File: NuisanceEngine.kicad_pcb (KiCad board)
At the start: 2 copper layers, 60 x 53 mm, 58 parts, among them J1 CV, J2 Headphones, J3 Power, Q1 2N3904, Q2 2N3904, Q3 TIP31A, Q4 TIP32A, SW1 SW_SPDT, SW2 SW_SPDT, U1 LM324

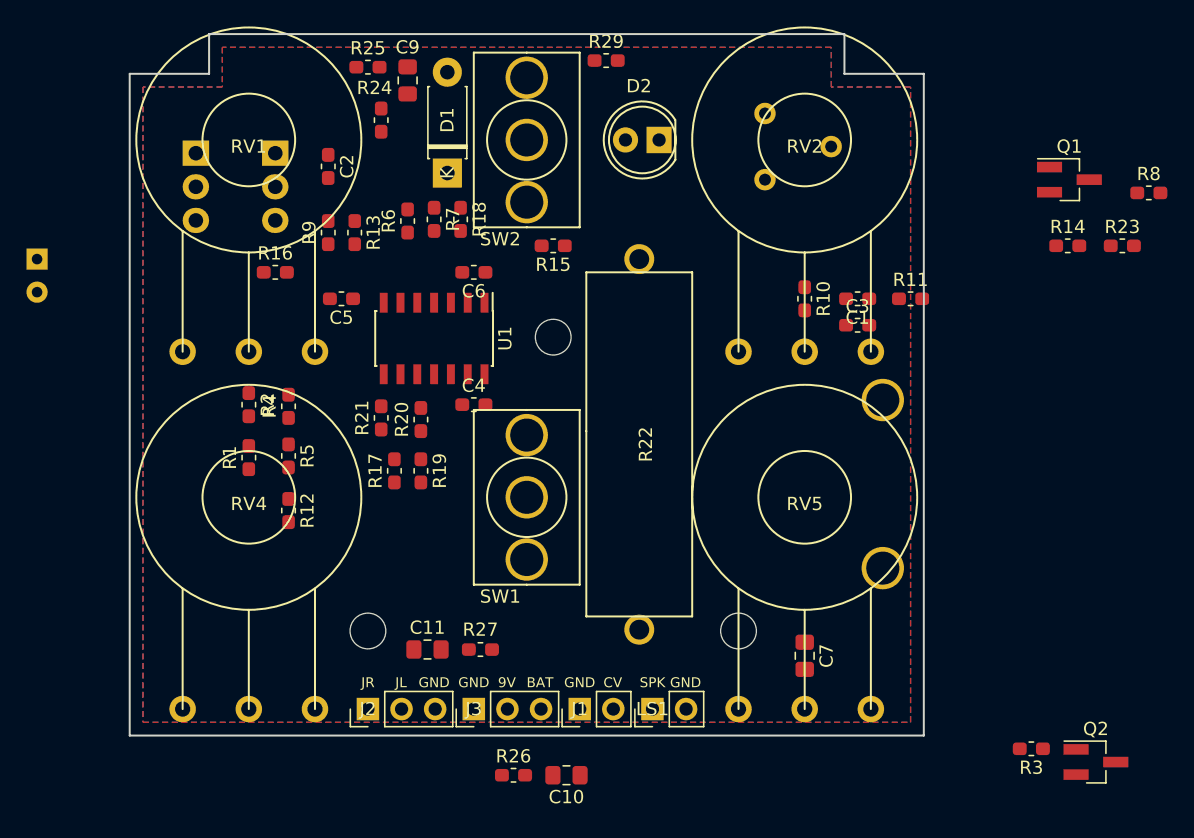
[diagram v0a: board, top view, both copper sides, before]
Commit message: Laid out SMT components, ready for traces
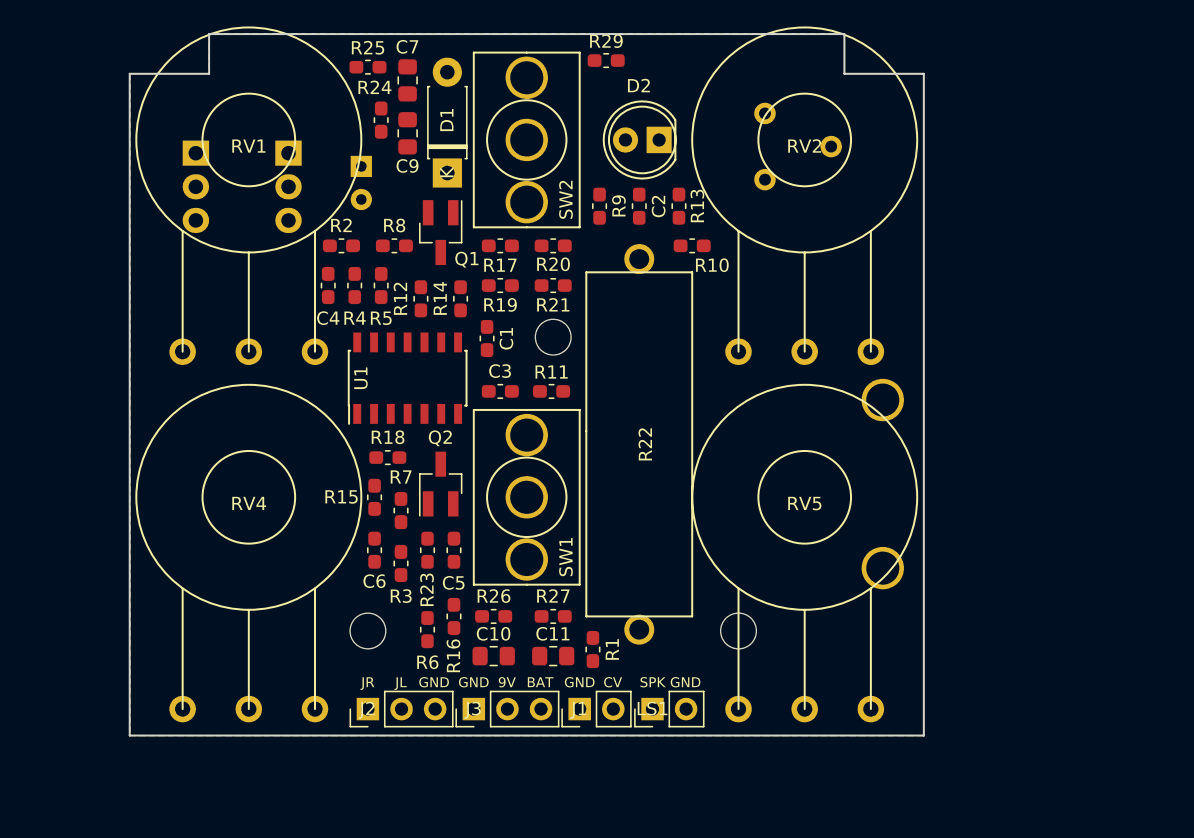
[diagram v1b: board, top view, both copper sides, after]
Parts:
- moved R23 57.3 mm to (72.5, 86.0), turned to 90 degrees
- moved R8 57.1 mm to (70.0, 63.0), turned to 180 degrees
- moved Q2 53.8 mm to (73.5, 81.0), turned to 90 degrees
- moved C7 52.8 mm to (71.0, 50.5), turned to 90 degrees
- moved R3 49.6 mm to (70.5, 87.0), turned to 270 degrees
- moved Q1 47.7 mm to (73.5, 62.0), turned to 270 degrees
- moved R14 46.0 mm to (75.0, 67.0), turned to 270 degrees
- moved R6 30.9 mm to (72.5, 92.0), turned to 270 degrees
- moved R1 29.8 mm to (85.0, 93.5)
- moved R16 29.3 mm to (74.5, 91.0), turned to 270 degrees
- moved C1 28.2 mm to (77.0, 70.0), turned to 90 degrees
- moved R11 28.0 mm to (81.9, 74.0)
- moved C3 27.5 mm to (78.0, 74.0)
- moved C8 25.5 mm to (67.5, 57.0)
- moved R13 24.6 mm to (91.5, 60.0)
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
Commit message: Dunzo
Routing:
- net Net-(C6-Pad1): track 0.00 -> 177.4 mm
- net Net-(C7-Pad2): track 0.00 -> 86.0 mm
- net Net-(C3-Pad1): track 0.00 -> 69.6 mm
- net VDD: track 0.00 -> 67.5 mm
- net Net-(C6-Pad2): track 0.00 -> 45.9 mm, vias 0 -> 2
- net Net-(J3-Pad2): track 0.00 -> 43.5 mm
- net Net-(R1-Pad2): track 0.00 -> 43.0 mm, vias 0 -> 2
- net Net-(BT1-Pad1): track 0.00 -> 36.2 mm
- net Net-(R22-Pad1): track 0.00 -> 35.6 mm
- net Net-(C4-Pad1): track 0.00 -> 35.6 mm
- net Net-(C1-Pad2): track 0.00 -> 32.4 mm
- net Net-(R14-Pad2): track 0.00 -> 31.9 mm, vias 0 -> 2
- net Net-(C8-Pad2): track 0.00 -> 27.7 mm
- net Net-(C7-Pad1): track 0.00 -> 22.6 mm
- net Net-(R3-Pad2): track 0.00 -> 20.3 mm
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
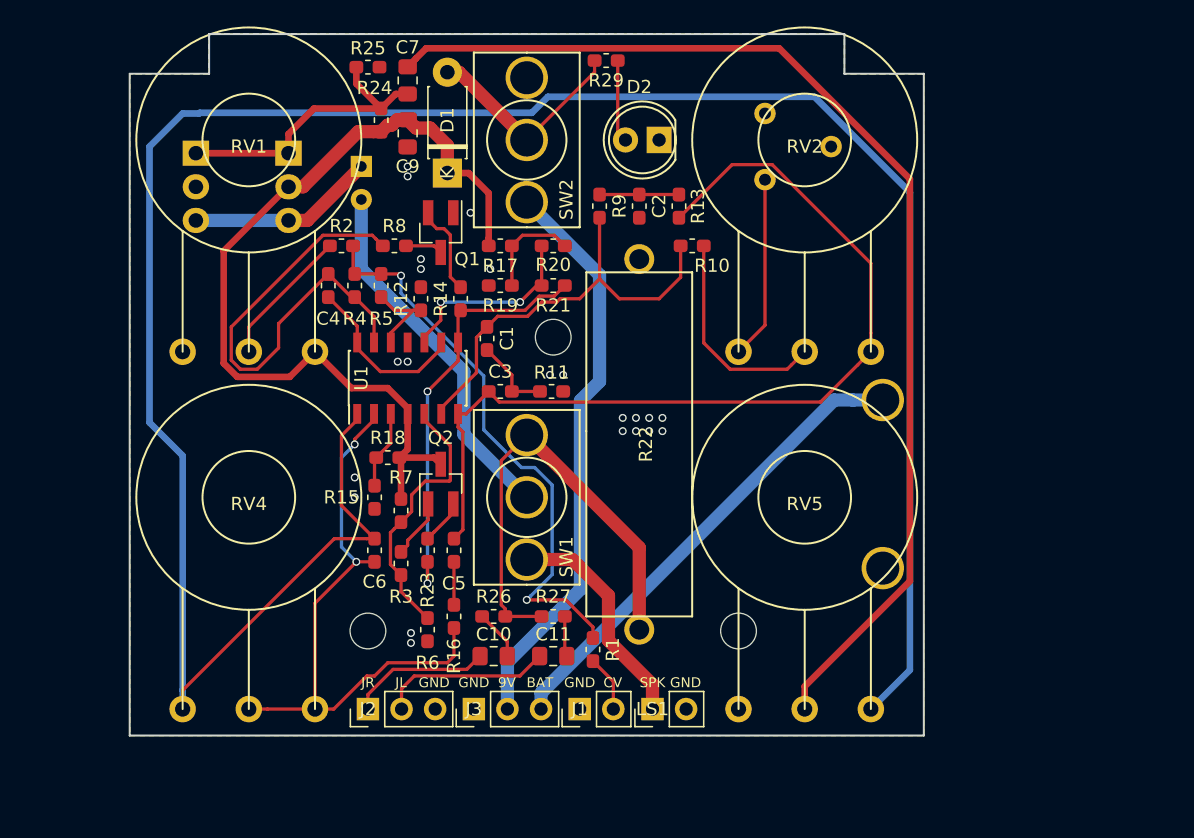
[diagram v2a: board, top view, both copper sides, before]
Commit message: Commit before changing pot footprint
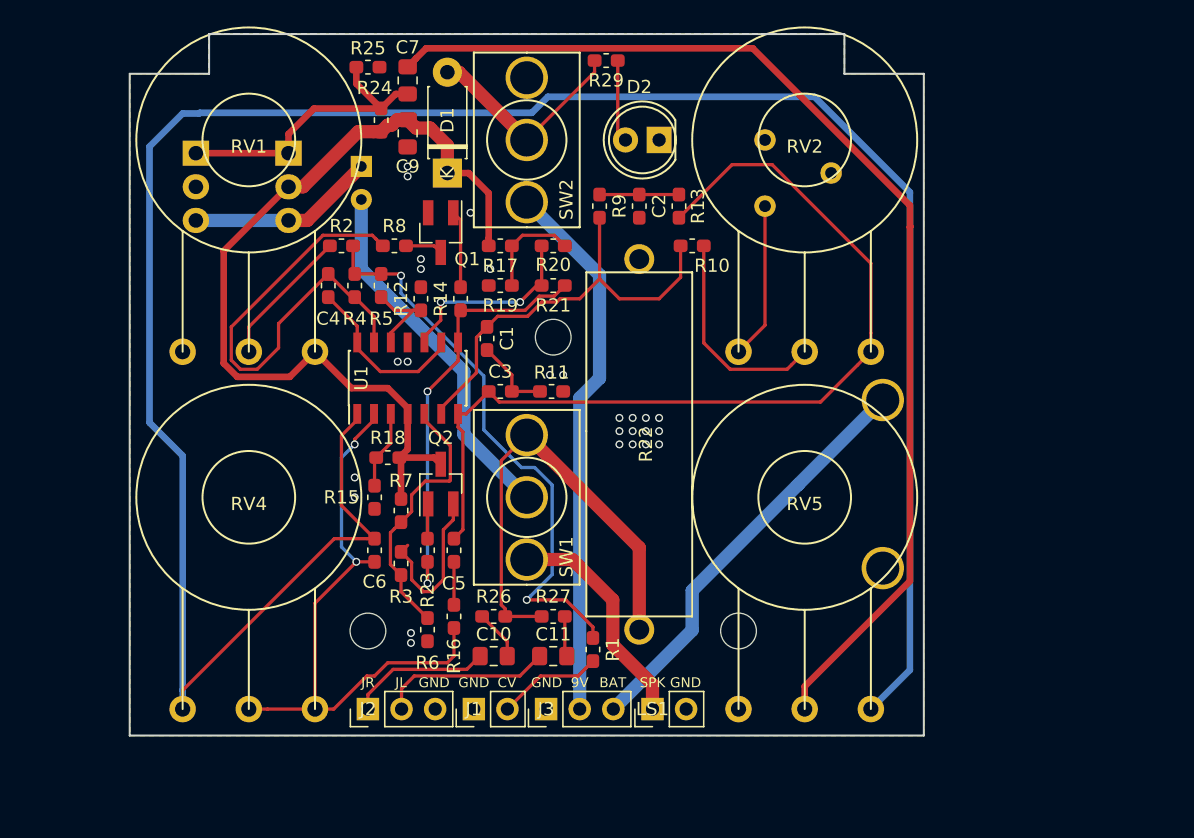
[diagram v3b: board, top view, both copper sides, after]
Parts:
- added LOGO: , HammerheadAudio:HHLOGO, B.Cu at (64.5, 47.5)
- C4: value .047uf -> 0.047uf
- moved J1 8.00 mm to (76.0, 98.0)
- moved J3 5.46 mm to (81.5, 98.0)
- moved RV3 2.00 mm to (98.0, 55.0)
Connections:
- Q1 pad 1: GND -> Net-(Q1-Pad1)
- Q1 pad 2: Net-(Q1-Pad2) -> GND
- R14 pad 1: Net-(Q1-Pad2) -> Net-(Q1-Pad1)
- R23 pad 2: Net-(Q2-Pad2) -> Net-(Q2-Pad1)
- R3 pad 1: Net-(Q2-Pad1) -> Net-(Q2-Pad2)
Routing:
- net Net-(Q2-Pad2): track 3.43 -> 13.0 mm
- net Net-(Q1-Pad2): track 6.96 -> 0.00 mm
- net Net-(Q1-Pad1): track 0.00 -> 5.85 mm
- net Net-(BT1-Pad1): track 36.2 -> 31.8 mm
- net Net-(J1-Pad2): track 4.26 -> 7.96 mm
- net Net-(J3-Pad2): track 43.5 -> 41.2 mm
- net Net-(RV2-Pad1): track 13.8 -> 11.8 mm
- net Net-(Q2-Pad1): track 4.47 -> 2.65 mm
- net Net-(C7-Pad2): track 86.0 -> 84.9 mm
- net GND: track 0.45 -> 1.00 mm, vias 22 -> 26
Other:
- board text added: "Adjust Min Resonance"
- board text added: "Nuisance Engine V1.0 Emmett Palaima Hammerhead Audio 2019"

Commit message: new pot footprint
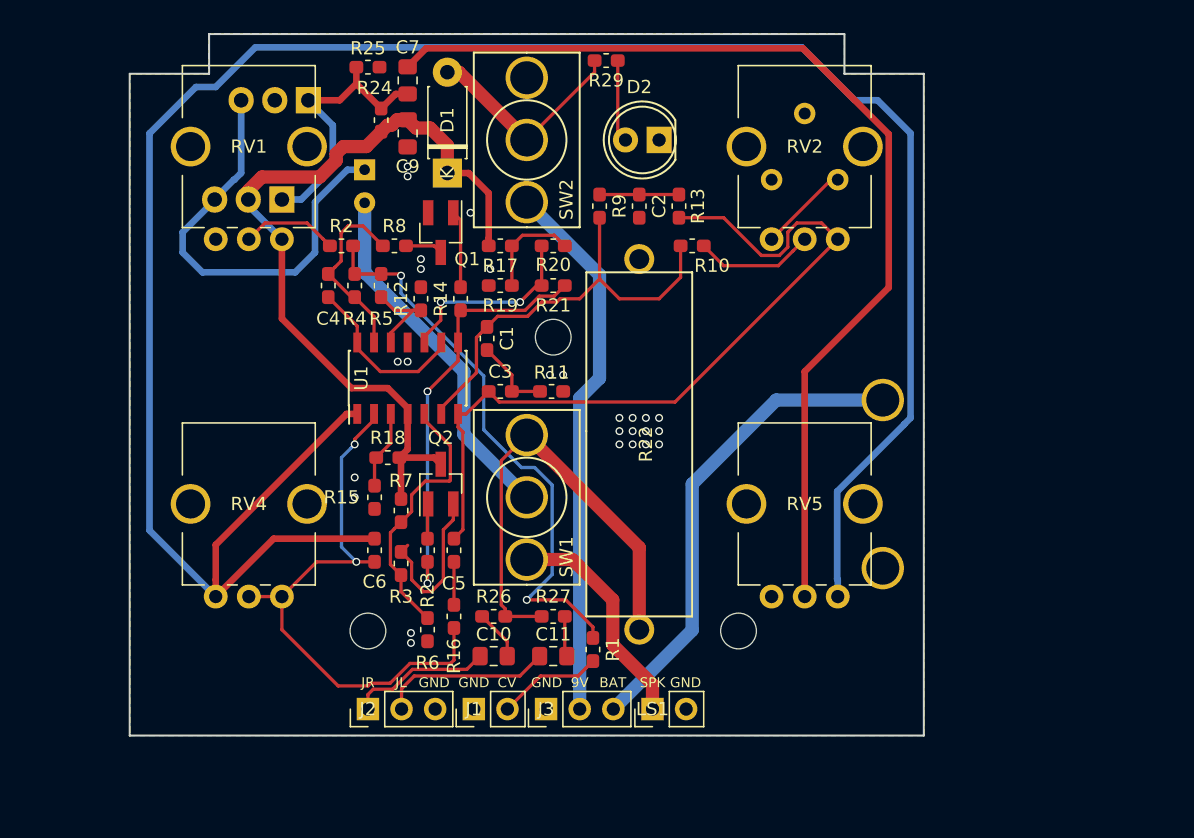
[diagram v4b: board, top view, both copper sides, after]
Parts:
- RV1, RV2, RV4, RV5: footprint HammerheadAudio:Alpha_Pot_16MM -> HammerheadAudio:PTV09
- moved Q4 9.39 mm to (63.5, 52.0), turned to 180 degrees
- moved Q3 3.54 mm to (61.5, 59.5), turned to 180 degrees
- moved RV3 3.04 mm to (98.5, 58.0), turned to 90 degrees
- moved C8 0.35 mm to (67.8, 57.2)
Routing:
- net Net-(C4-Pad1): track 35.6 -> 14.2 mm
- net Net-(C8-Pad1): track 14.2 -> 33.2 mm
- net Net-(C3-Pad1): track 69.6 -> 60.0 mm
- net Net-(C7-Pad2): track 84.9 -> 77.2 mm
- net Net-(C6-Pad1): track 177.4 -> 169.8 mm
- net Net-(R10-Pad2): track 16.3 -> 9.07 mm
- net VDD: track 67.5 -> 61.7 mm
- net Net-(RV2-Pad1): track 11.8 -> 6.86 mm
- net Net-(BT1-Pad1): track 31.8 -> 36.5 mm
- net Net-(R2-Pad1): track 10.5 -> 7.35 mm
- net Net-(C6-Pad2): track 45.9 -> 43.9 mm
- net Net-(C7-Pad1): track 22.6 -> 21.2 mm
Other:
- board text added: "Nuisance Engine V1.1 Emmett Palaima Hammerhead Audio 2019"
- board text removed: "Nuisance Engine V1.0 Emmett Palaima Hammerhead Audio 2019"
